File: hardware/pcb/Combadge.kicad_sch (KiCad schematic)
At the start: 19 parts, among them J1 Conn_01x05_Female, J3 TOUCH, U2 ESP32-WROOM-32, U4 MAX98357AEWL+T

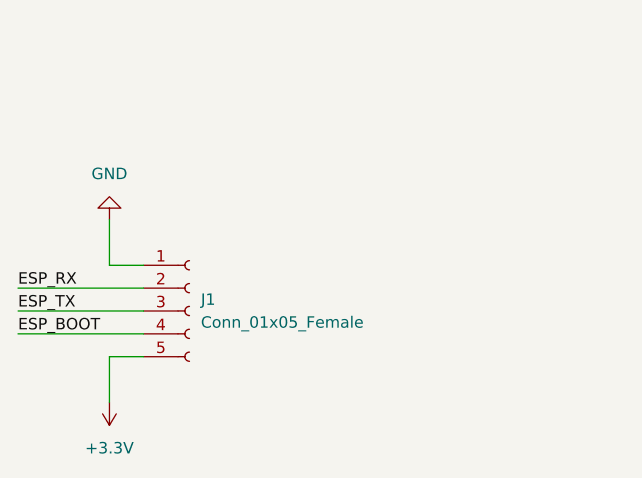
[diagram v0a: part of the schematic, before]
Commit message: Add power switch and rework header placement
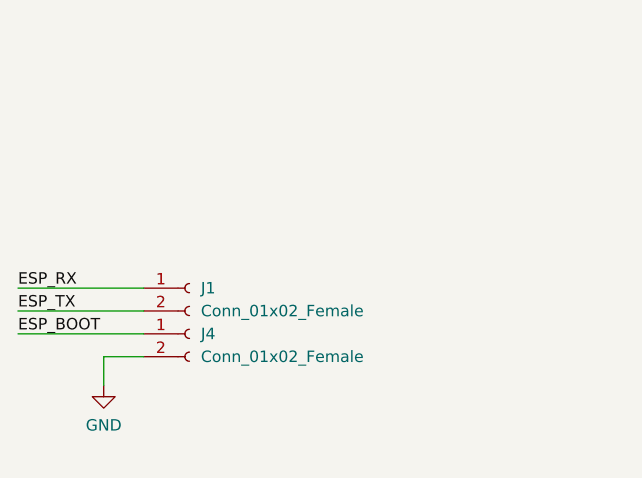
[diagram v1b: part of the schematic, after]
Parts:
- removed J1: Conn_01x05_Female, Connector_PinHeader_2.54mm:PinHeader_1x05_P2.54mm_Vertical, symbol Connector:Conn_01x05_Female
- added J1, J4: Conn_01x02_Female, Connector_PinHeader_2.54mm:PinHeader_1x02_P2.54mm_Vertical, symbol Connector:Conn_01x02_Female
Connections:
- net ESP_BOOT: now also J4.1 (Pin_1)
- net ESP_RX: now also J1.1 (Pin_1)
- net ESP_TX: now also J1.2 (Pin_2)
- net GND: now also J4.2 (Pin_2)
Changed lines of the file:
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@@
-    (stroke (width 0) (type default) (color 0 0 0 0))
-  )
-  (wire (pts (xy 30.48 173.99) (xy 34.29 173.99))
     (stroke (width 0) (type default) (color 0 0 0 0))
   )
@@
     (stroke (width 0) (type default) (color 0 0 0 0))
   )
-  (wire (pts (xy 34.29 184.15) (xy 30.48 184.15))
+  (wire (pts (xy 34.29 184.15) (xy 29.845 184.15))
     (stroke (width 0) (type default) (color 0 0 0 0))
   )
@@
     (stroke (width 0) (type default) (color 0 0 0 0))
   )
+  (wire (pts (xy 29.845 184.15) (xy 29.845 187.325))
+    (stroke (width 0) (type default) (color 0 0 0 0))
+  )
   (wire (pts (xy 20.32 181.61) (xy 34.29 181.61))
     (stroke (width 0) (type default) (color 0 0 0 0))
@@
     (stroke (width 0) (type default) (color 0 0 0 0))
   )
-  (wire (pts (xy 30.48 168.91) (xy 30.48 173.99))
-    (stroke (width 0) (type default) (color 0 0 0 0))
-  )
   (wire (pts (xy 250.19 148.59) (xy 264.16 148.59))
     (stroke (width 0) (type default) (color 0 0 0 0))
@@
   )
   (wire (pts (xy 88.9 55.88) (xy 106.68 55.88))
-    (stroke (width 0) (type default) (color 0 0 0 0))
-  )
-  (wire (pts (xy 30.48 184.15) (xy 30.48 189.23))
     (stroke (width 0) (type default) (color 0 0 0 0))
   )
@@
     (pin "1")
   )
-  (symbol (lib_id "power:GND") (at 30.48 168.91 180) (unit 1)
-    (in_bom yes) (on_board yes) (fields_autoplaced)
-    (property "Reference" "#PWR0105" (id 0) (at 30.48 162.56 0)
-      (effects (font (size 1.27 1.27)) hide)
-    )
-    (property "Value" "GND" (id 1) (at 30.48 163.83 0))
-    (property "Footprint" "" (id 2) (at 30.48 168.91 0)
-      (effects (font (size 1.27 1.27)) hide)
-    )
-    (property "Datasheet" "" (id 3) (at 30.48 168.91 0)
+  (symbol (lib_id "power:GND") (at 29.845 187.325 0) (unit 1)
+    (in_bom yes) (on_board yes) (fields_autoplaced)
+    (property "Reference" "#PWR0105" (id 0) (at 29.845 193.675 0)
+      (effects (font (size 1.27 1.27)) hide)
+    )
+    (property "Value" "GND" (id 1) (at 29.845 191.77 0))
+    (property "Footprint" "" (id 2) (at 29.845 187.325 0)
+      (effects (font (size 1.27 1.27)) hide)
+    )
+    (property "Datasheet" "" (id 3) (at 29.845 187.325 0)
       (effects (font (size 1.27 1.27)) hide)
     )
@@
     (pin "9")
   )
-  (symbol (lib_id "Connector:Conn_01x05_Female") (at 39.37 179.07 0) (unit 1)
-    (in_bom yes) (on_board yes) (fields_autoplaced)
-    (property "Reference" "J1" (id 0) (at 40.64 177.7999 0)
-      (effects (font (size 1.27 1.27)) (justify left))
-    )
-    (property "Value" "Conn_01x05_Female" (id 1) (at 40.64 180.3399 0)
-      (effects (font (size 1.27 1.27)) (justify left))
-    )
-    (property "Footprint" "Connector_PinHeader_2.54mm:PinHeader_1x05_P2.54mm_Vertical" (id 2) (at 39.37 179.07 0)
-      (effects (font (size 1.27 1.27)) hide)
-    )
-    (property "Datasheet" "~" (id 3) (at 39.37 179.07 0)
-      (effects (font (size 1.27 1.27)) hide)
-    )
-    (pin "1")
-    (pin "2")
-    (pin "3")
-    (pin "4")
-    (pin "5")
+  (symbol (lib_id "Connector:Conn_01x02_Female") (at 39.37 176.53 0) (unit 1)
+    (in_bom yes) (on_board yes) (fields_autoplaced)
+    (property "Reference" "J1" (id 0) (at 40.64 176.5299 0)
+      (effects (font (size 1.27 1.27)) (justify left))
+    )
+    (property "Value" "Conn_01x02_Female" (id 1) (at 40.64 179.0699 0)
+      (effects (font (size 1.27 1.27)) (justify left))
+    )
+    (property "Footprint" "Connector_PinHeader_2.54mm:PinHeader_1x02_P2.54mm_Vertical" (id 2) (at 39.37 176.53 0)
+      (effects (font (size 1.27 1.27)) hide)
+    )
+    (property "Datasheet" "~" (id 3) (at 39.37 176.53 0)
+      (effects (font (size 1.27 1.27)) hide)
+    )
+    (pin "1")
+    (pin "2")
+  )
+  (symbol (lib_id "Connector:Conn_01x02_Female") (at 39.37 181.61 0) (unit 1)
+    (in_bom yes) (on_board yes) (fields_autoplaced)
+    (property "Reference" "J4" (id 0) (at 40.64 181.6099 0)
+      (effects (font (size 1.27 1.27)) (justify left))
+    )
+    (property "Value" "Conn_01x02_Female" (id 1) (at 40.64 184.1499 0)
+      (effects (font (size 1.27 1.27)) (justify left))
+    )
+    (property "Footprint" "Connector_PinHeader_2.54mm:PinHeader_1x02_P2.54mm_Vertical" (id 2) (at 39.37 181.61 0)
+      (effects (font (size 1.27 1.27)) hide)
+    )
+    (property "Datasheet" "~" (id 3) (at 39.37 181.61 0)
+      (effects (font (size 1.27 1.27)) hide)
+    )
+    (pin "1")
+    (pin "2")
   )
   (symbol (lib_id "Device:C") (at 50.8 26.67 90) (unit 1)
@@
     (pin "1")
   )
-  (symbol (lib_id "power:+3.3V") (at 30.48 189.23 180) (unit 1)
-    (in_bom yes) (on_board yes) (fields_autoplaced)
-    (property "Reference" "#PWR0103" (id 0) (at 30.48 185.42 0)
-      (effects (font (size 1.27 1.27)) hide)
-    )
-    (property "Value" "+3.3V" (id 1) (at 30.48 194.31 0))
-    (property "Footprint" "" (id 2) (at 30.48 189.23 0)
-      (effects (font (size 1.27 1.27)) hide)
-    )
-    (property "Datasheet" "" (id 3) (at 30.48 189.23 0)
-      (effects (font (size 1.27 1.27)) hide)
-    )
-    (pin "1")
-  )
   (symbol (lib_id "Device:C") (at 264.16 24.13 0) (unit 1)
     (in_bom yes) (on_board yes) (fields_autoplaced)
@@
       (reference "#PWR0102") (unit 1) (value "+3.3V") (footprint "")
     )
-    (path "/ad0ae77d-d38c-4ba1-b039-bc8687896d21"
-      (reference "#PWR0103") (unit 1) (value "+3.3V") (footprint "")
-    )
     (path "/20a761e7-e64c-4e12-8a9a-c571b59ad452"
       (reference "#PWR0104") (unit 1) (value "GND") (footprint "")
@@
       (reference "D1") (unit 1) (value "D_Zener_Dual_CommonAnode_KKA") (footprint "Package_TO_SOT_SMD:SOT-23")
     )
-    (path "/a1162625-0ef3-4f3c-9db9-a306a20d12d7"
-      (reference "J1") (unit 1) (value "Conn_01x05_Female") (footprint "Connector_PinHeader_2.54mm:PinHeader_1x05_P2.54mm_Vertical")
+    (path "/94088ca5-43a2-408d-8654-992b6e945d84"
+      (reference "J1") (unit 1) (value "Conn_01x02_Female") (footprint "Connector_PinHeader_2.54mm:PinHeader_1x02_P2.54mm_Vertical")
     )
     (path "/522738f4-f6b2-4897-a079-07da122bd152/54bad96c-0bd2-4df6-9bda-0db6ccbaa90e"
@@
       (reference "J3") (unit 1) (value "TOUCH") (footprint "Connector_PinHeader_2.54mm:PinHeader_1x01_P2.54mm_Vertical")
     )
+    (path "/9d4d1604-a3fc-4dca-b3fb-d78228d696a1"
+      (reference "J4") (unit 1) (value "Conn_01x02_Female") (footprint "Connector_PinHeader_2.54mm:PinHeader_1x02_P2.54mm_Vertical")
+    )
     (path "/17cf851e-baf5-4a53-b51d-b404d181f43d"
       (reference "LS1") (unit 1) (value "Speaker") (footprint "Connector_PinHeader_2.54mm:PinHeader_1x02_P2.54mm_Vertical")
@@
       (reference "R_ISET1") (unit 1) (value "10k") (footprint "Resistor_SMD:R_1206_3216Metric_Pad1.30x1.75mm_HandSolder")
     )
-    (path "/522738f4-f6b2-4897-a079-07da122bd152/b0be4319-86de-42e4-aed3-d046aae94521"
-      (reference "SW1") (unit 1) (value "SW_SPST") (footprint "")
+    (path "/522738f4-f6b2-4897-a079-07da122bd152/2bcb8ba2-2cfb-4784-92a6-ce27ddcfec7e"
+      (reference "SW1") (unit 1) (value "CSS-1210TB") (footprint "CSS-1210TB:CSS-1210TB")
     )
     (path "/522738f4-f6b2-4897-a079-07da122bd152/4d9bfdc9-548c-473b-8b63-b9edd4d05e1e"
@@
     )
     (path "/522738f4-f6b2-4897-a079-07da122bd152/30504c5d-3679-41ee-b2c5-c1db3e0d5443"
-      (reference "U5") (unit 1) (value "RN4989") (footprint "SOT-363   US6_TOS")
-    )
-  )
+      (reference "U5") (unit 1) (value "RN4989") (footprint "RN4989:RN4989")
+    )
+  )

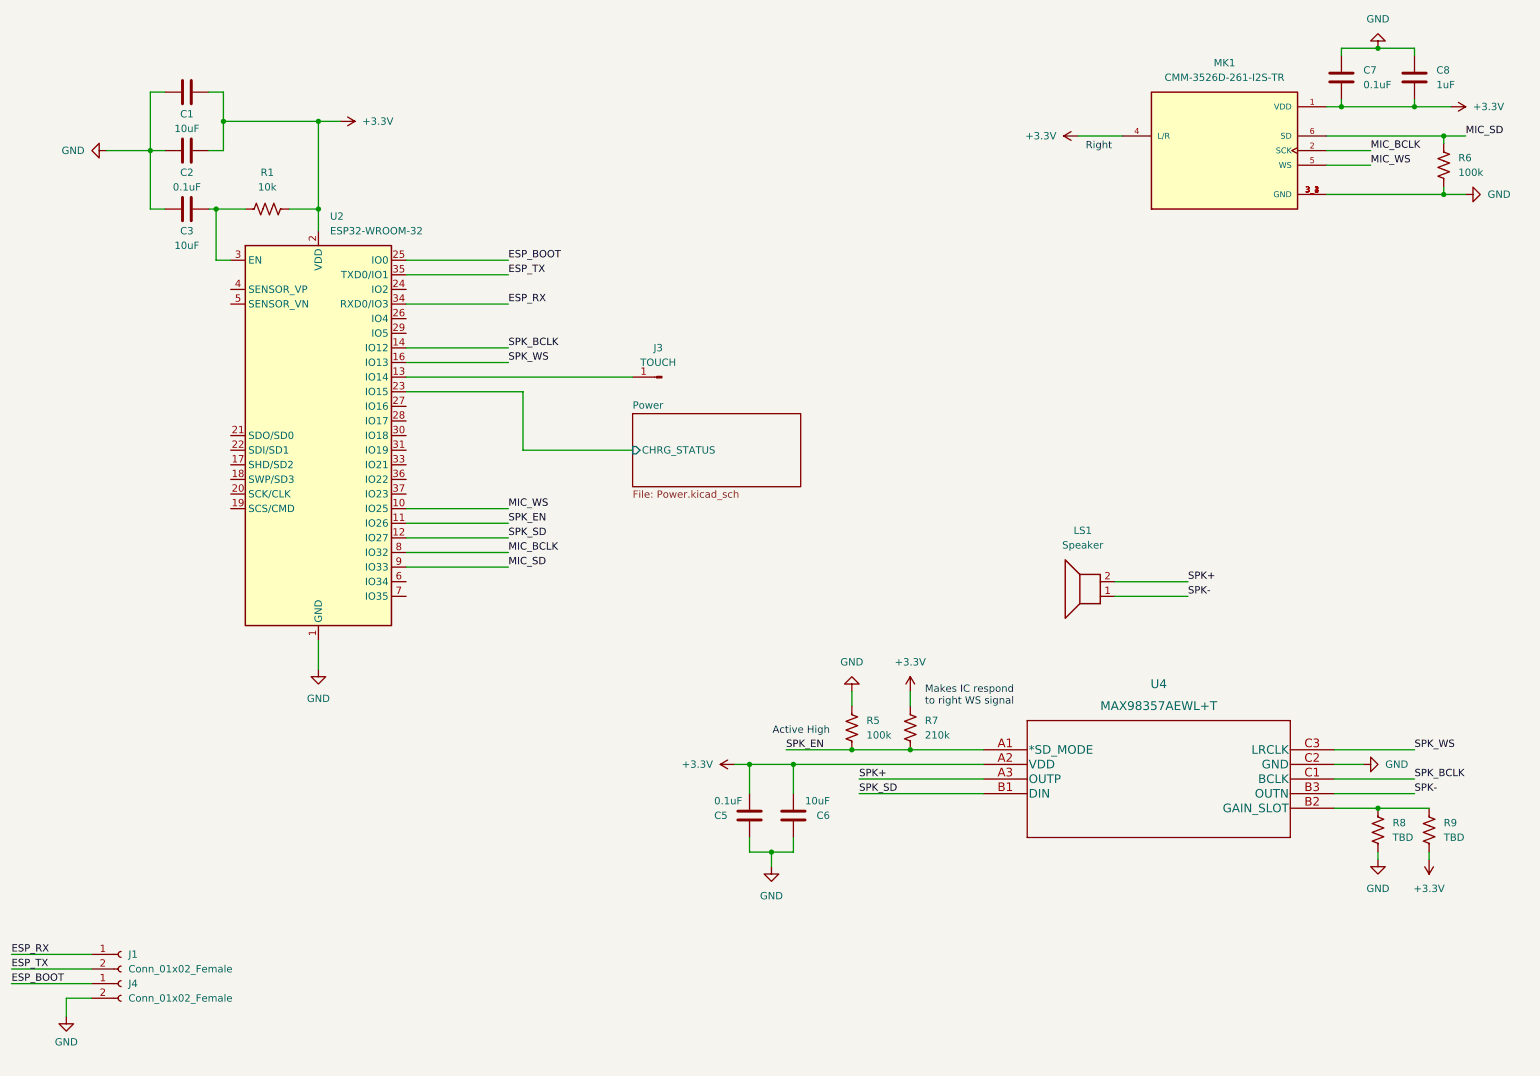
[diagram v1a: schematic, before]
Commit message: Flatten edge of PCB where micro USB port sits
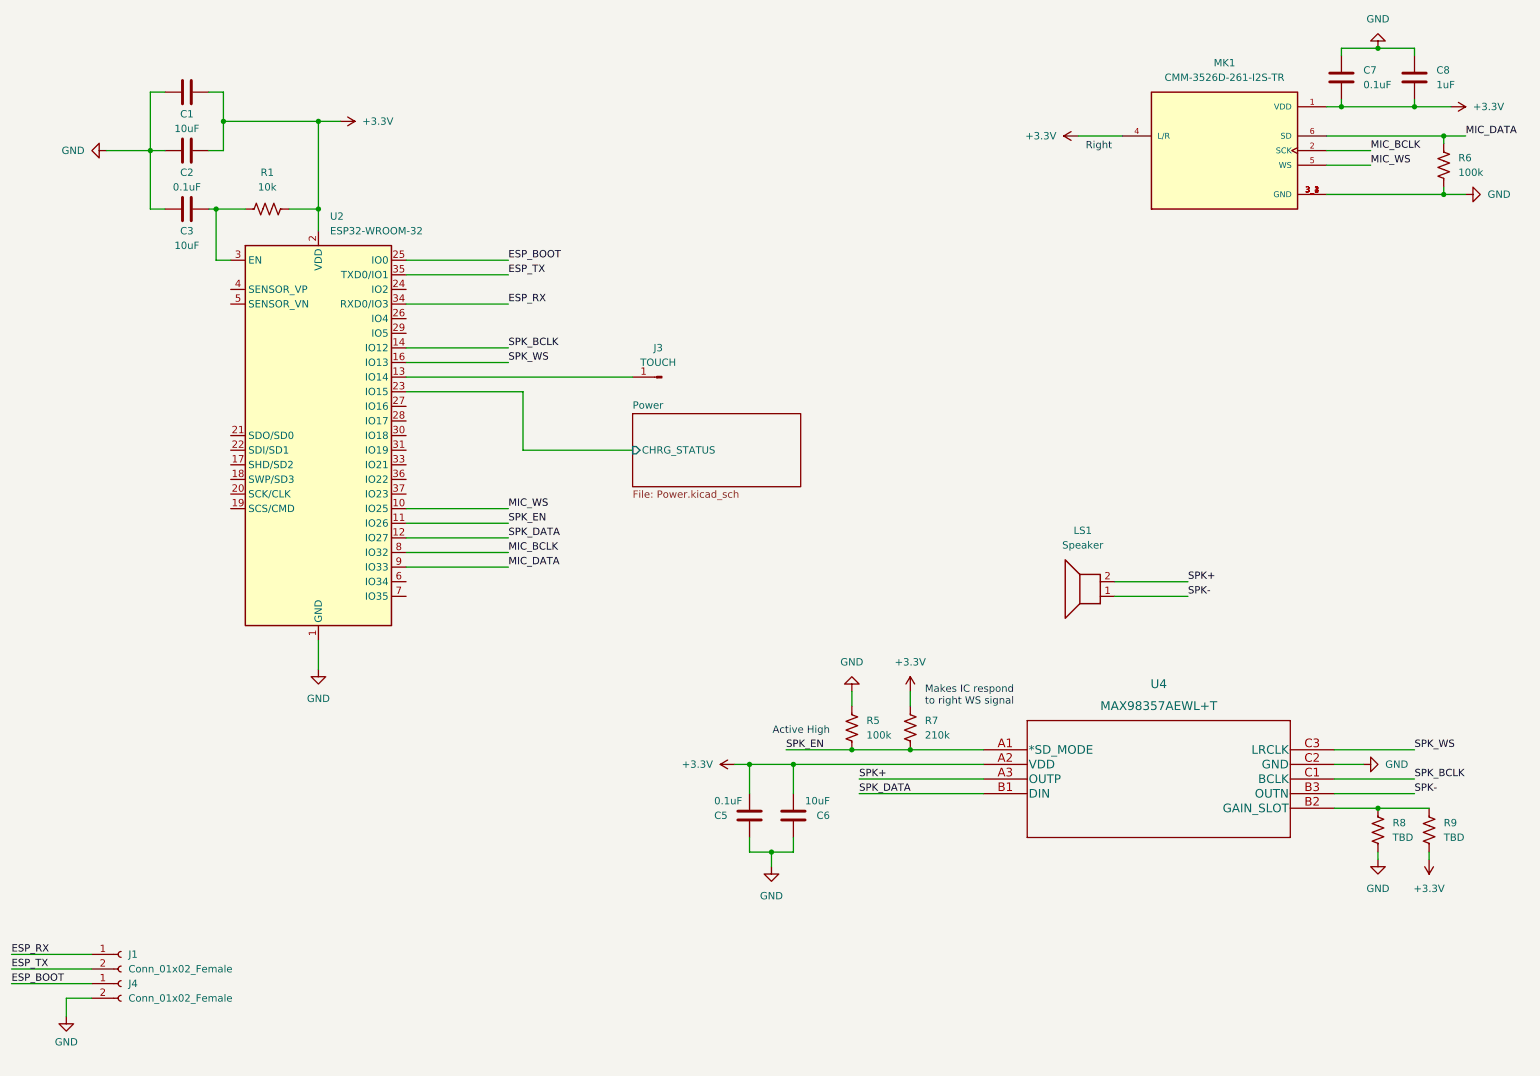
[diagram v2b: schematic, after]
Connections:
- net MIC_SD renamed MIC_DATA
- net SPK_SD renamed SPK_DATA
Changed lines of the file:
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@@
     (effects (font (size 1.27 1.27)) (justify left bottom))
   )
-  (label "MIC_SD" (at 273.05 34.29 0)
+  (label "MIC_DATA" (at 273.05 34.29 0)
     (effects (font (size 1.27 1.27)) (justify left bottom))
   )
@@
     (effects (font (size 1.27 1.27)) (justify left bottom))
   )
-  (label "SPK_SD" (at 167.64 148.59 0)
+  (label "SPK_DATA" (at 167.64 148.59 0)
     (effects (font (size 1.27 1.27)) (justify left bottom))
   )
@@
     (effects (font (size 1.27 1.27)) (justify left bottom))
   )
-  (label "MIC_SD" (at 106.68 109.22 0)
+  (label "MIC_DATA" (at 106.68 109.22 0)
     (effects (font (size 1.27 1.27)) (justify left bottom))
   )
@@
     (effects (font (size 1.27 1.27)) (justify left bottom))
   )
-  (label "SPK_SD" (at 106.68 104.14 0)
+  (label "SPK_DATA" (at 106.68 104.14 0)
     (effects (font (size 1.27 1.27)) (justify left bottom))
   )

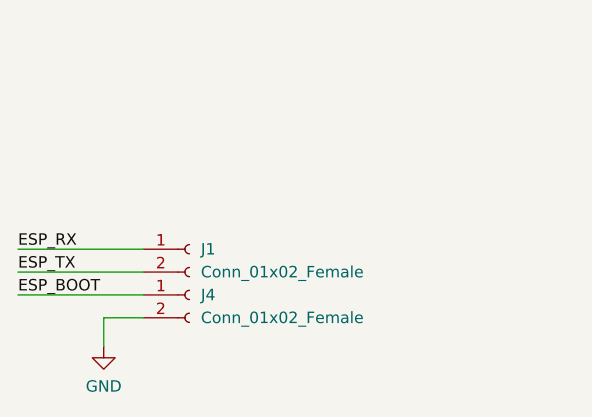
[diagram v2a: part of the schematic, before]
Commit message: Bump KiCad version to 7
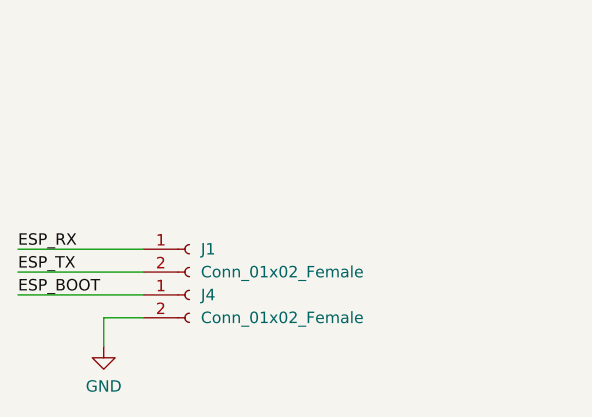
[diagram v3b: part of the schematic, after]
